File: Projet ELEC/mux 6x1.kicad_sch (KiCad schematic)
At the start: 13 parts, among them U1 74LS04, U2 74LS21, U3 74LS21, U4 74LS21, U5 74LS21, U6 4071, U7 4071

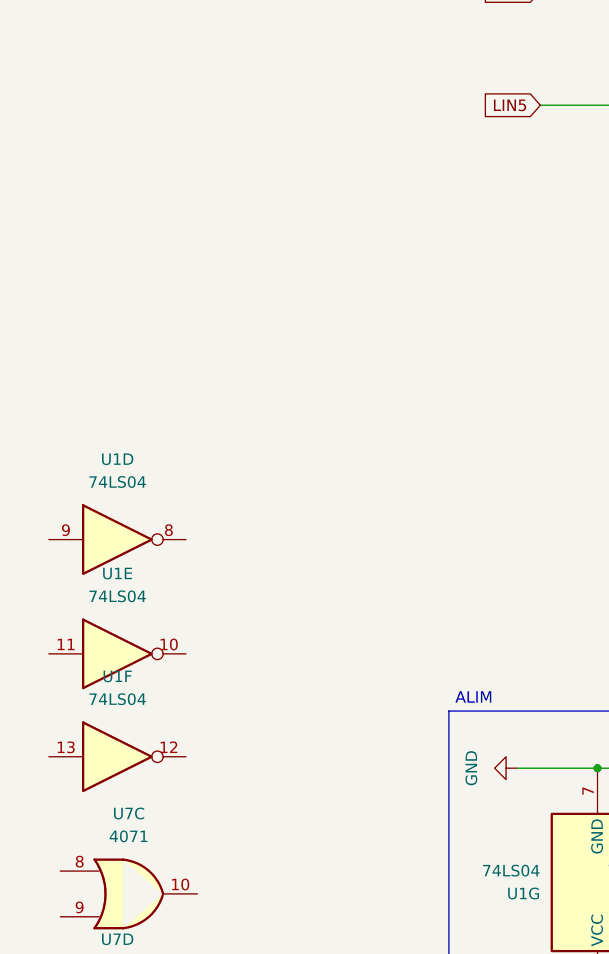
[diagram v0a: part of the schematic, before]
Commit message: corrected around 60 errors, removed a 74ls04, and many other improvements
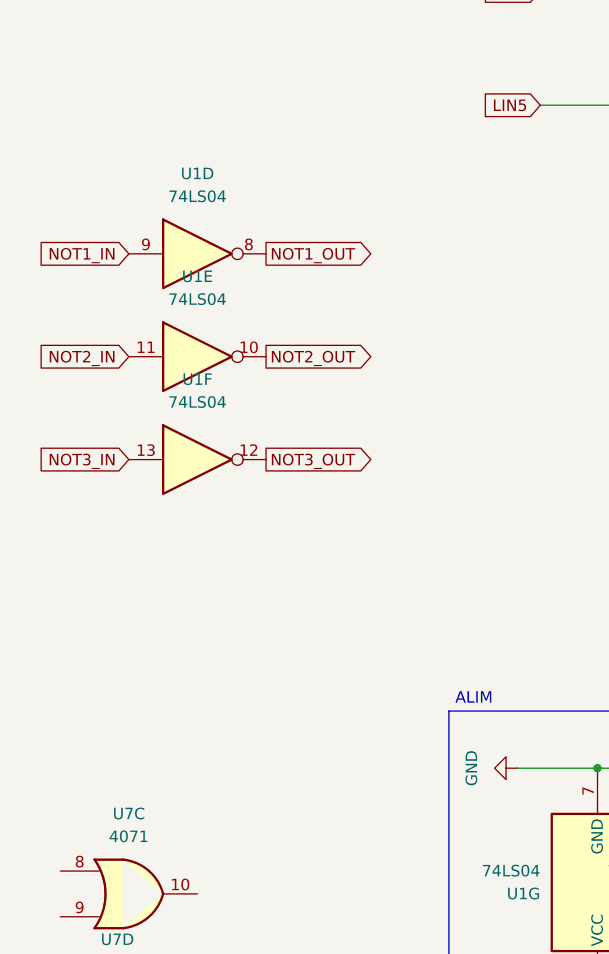
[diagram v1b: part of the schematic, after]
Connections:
- net NOT1_OUT: now reaches U1.8
- net NOT1_IN: now reaches U1.9
- net NOT2_OUT: now reaches U1.10
- net NOT2_IN: now reaches U1.11
- net NOT3_OUT: now reaches U1.12
- net NOT3_IN: now reaches U1.13
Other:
- moved on the sheet: U1D, U1E, U1F

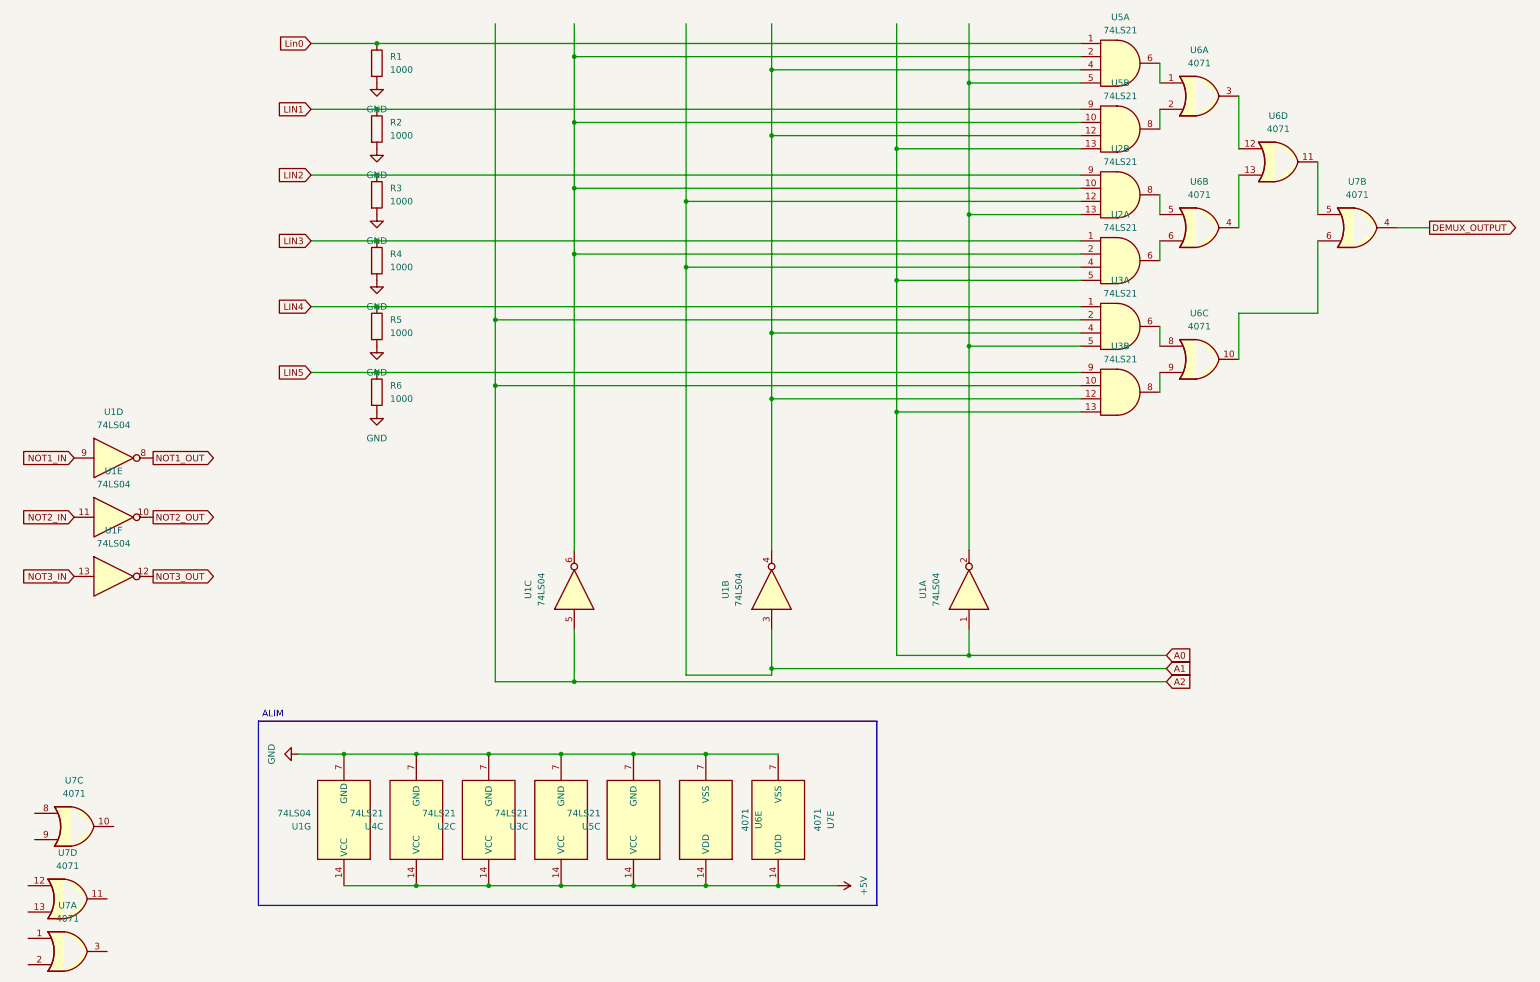
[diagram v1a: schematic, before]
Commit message: [~] not gates -> mosfet N
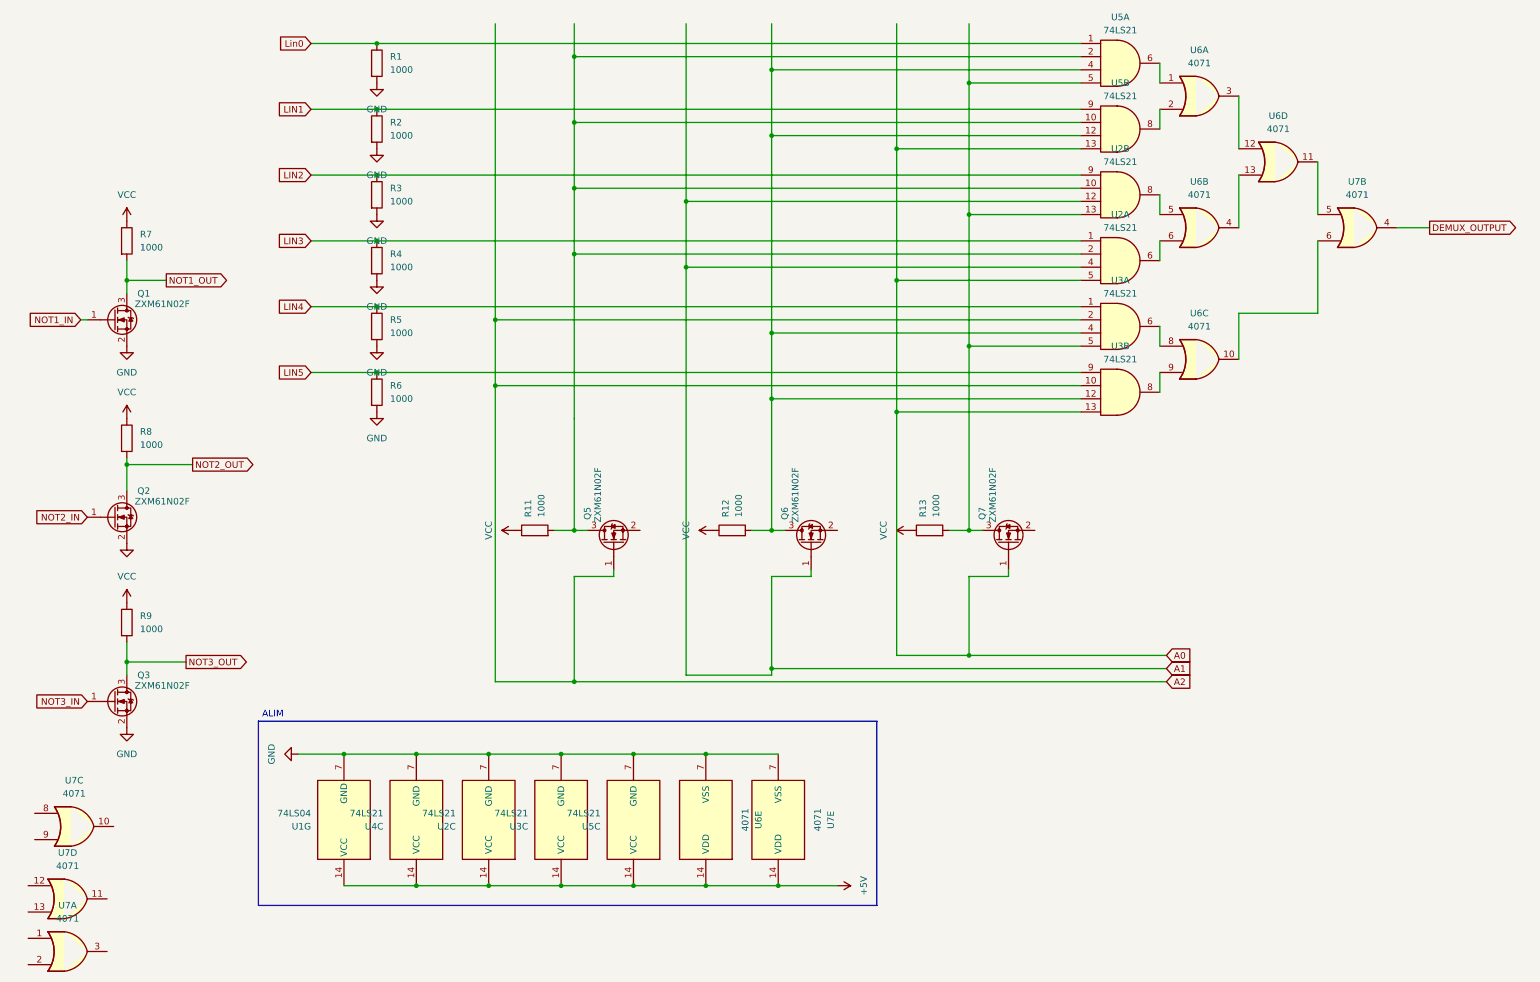
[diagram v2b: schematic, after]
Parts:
- removed unit 4 of U1
- removed unit 3 of U1
- removed unit 2 of U1
- removed unit 5 of U1
- removed unit 1 of U1
- removed unit 6 of U1
- added Q1, Q2, Q3, Q5, Q6, Q7: ZXM61N02F, Package_TO_SOT_SMD:SOT-23, symbol Transistor_FET:ZXM61N02F
- added R11, R12, R13, R7, R8, R9: 1000, symbol Device:R
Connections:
- net A0: now also Q7.1 (G)
- net A1: now also Q6.1 (G)
- net A2: now also Q5.1 (G)
- net GND: now also Q1.2 (S), Q2.2 (S), Q3.2 (S)
- net NOT1_IN: now also Q1.1 (G)
- net NOT1_OUT: now also Q1.3 (D), R7.2
- net NOT2_IN: now also Q2.1 (G)
- net NOT2_OUT: now also Q2.3 (D), R8.2
- net NOT3_IN: now also Q3.1 (G)
- net NOT3_OUT: now also Q3.3 (D), R9.2
- net at U3.12, U3.4, U5.12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: now also Q6.3 (D), R12.2
- net at U2.13, U3.5, U5.5: now also Q7.3 (D), R13.2
- net at U2.10, U2.2, U5.10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: now also Q5.3 (D), R11.2
- new net VCC: R11.1, R12.1, R13.1, R7.1, R8.1, R9.1

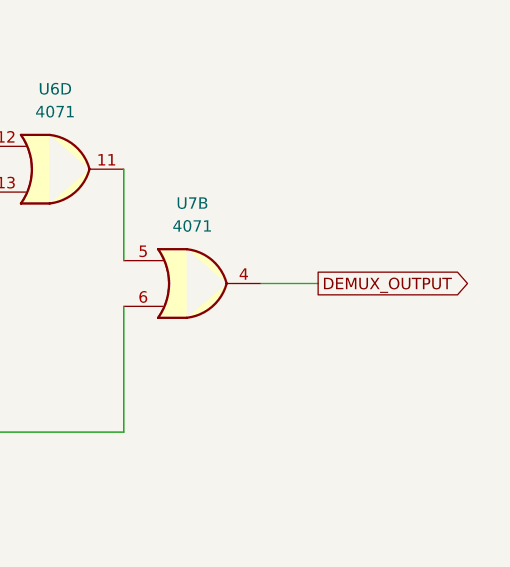
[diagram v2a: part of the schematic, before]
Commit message: fix(mux): rename mux output
* Projet ELEC/mux 6x1.kicad_sch
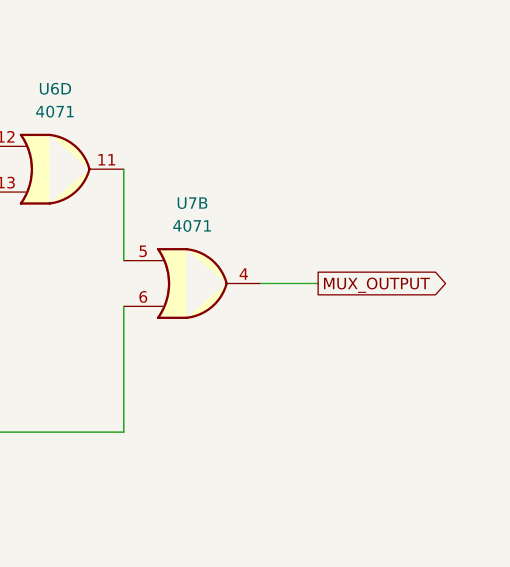
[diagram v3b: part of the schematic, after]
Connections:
- net DEMUX_OUTPUT renamed MUX_OUTPUT
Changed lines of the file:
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@@
 		)
 	)
-	(global_label "DEMUX_OUTPUT"
+	(global_label "MUX_OUTPUT"
 		(shape output)
 		(at 283.21 54.61 0)
@@
 		)
 		(property "Intersheetrefs" "${INTERSHEET_REFS}"
-			(at 300.7699 54.61 0)
+			(at 298.3509 54.61 0)
 			(effects
 				(font
